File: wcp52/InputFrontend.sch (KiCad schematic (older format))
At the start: 6 parts

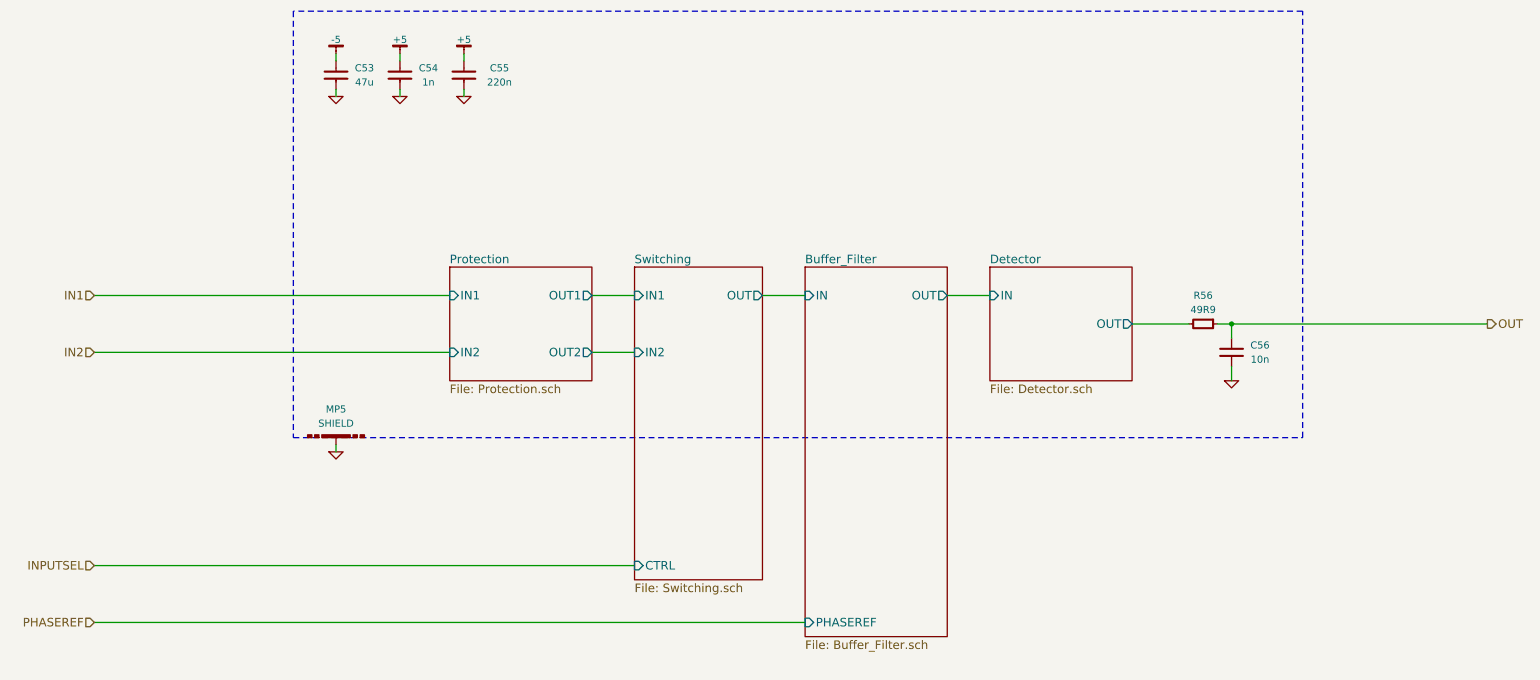
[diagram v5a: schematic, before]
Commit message: Change schematic pages to letter size
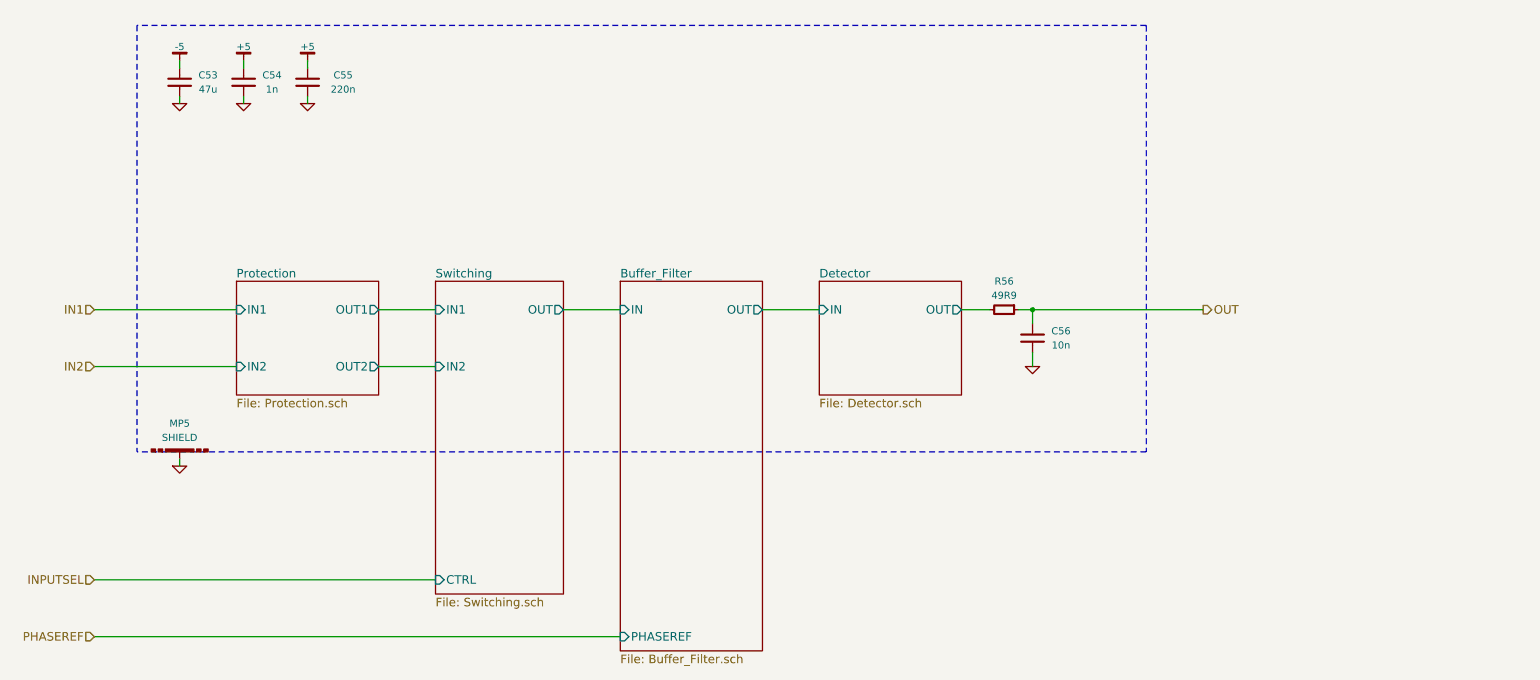
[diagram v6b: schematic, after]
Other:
- moved on the sheet: C53, C54, C55, C56, MP5, R56

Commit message: Correct BOM lines
The BOM reader currently cannot interpret things like '3k3'.
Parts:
- R56: BOM RES SMD 49R9 1% [0603] -> RES SMD 49.9 1% [0603]
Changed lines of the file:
@@
 F 3 "" H 8200 3350 60  0000 C CNN
 F 4 "Value" H 8200 3300 60  0001 C CNN "Manuf"
-F 5 "RES SMD 49R9 1% [0603]" H 8950 3850 60  0001 C CNN "BOM"
+F 5 "RES SMD 49.9 1% [0603]" H 8950 3850 60  0001 C CNN "BOM"
 F 6 "R52" H 8200 3300 50  0001 C CNN "OldReference"
 	1    8200 3300
